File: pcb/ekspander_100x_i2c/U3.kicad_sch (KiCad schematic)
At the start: 21 parts, among them J10 DG127A-5.08-06P-14-00AH, J11 DG127A-5.08-06P-14-00AH, J8 DG127A-5.08-06P-14-00AH, J9 DG127A-5.08-06P-14-00AH, U19 LTV-847, U20 LTV-847, U21 ITS716G, U22 ITS716G, U23 ITS716G, U24 ITS716G, U25 LTV-847, U3 MCP23017_SP, U4 MCP23017_SP

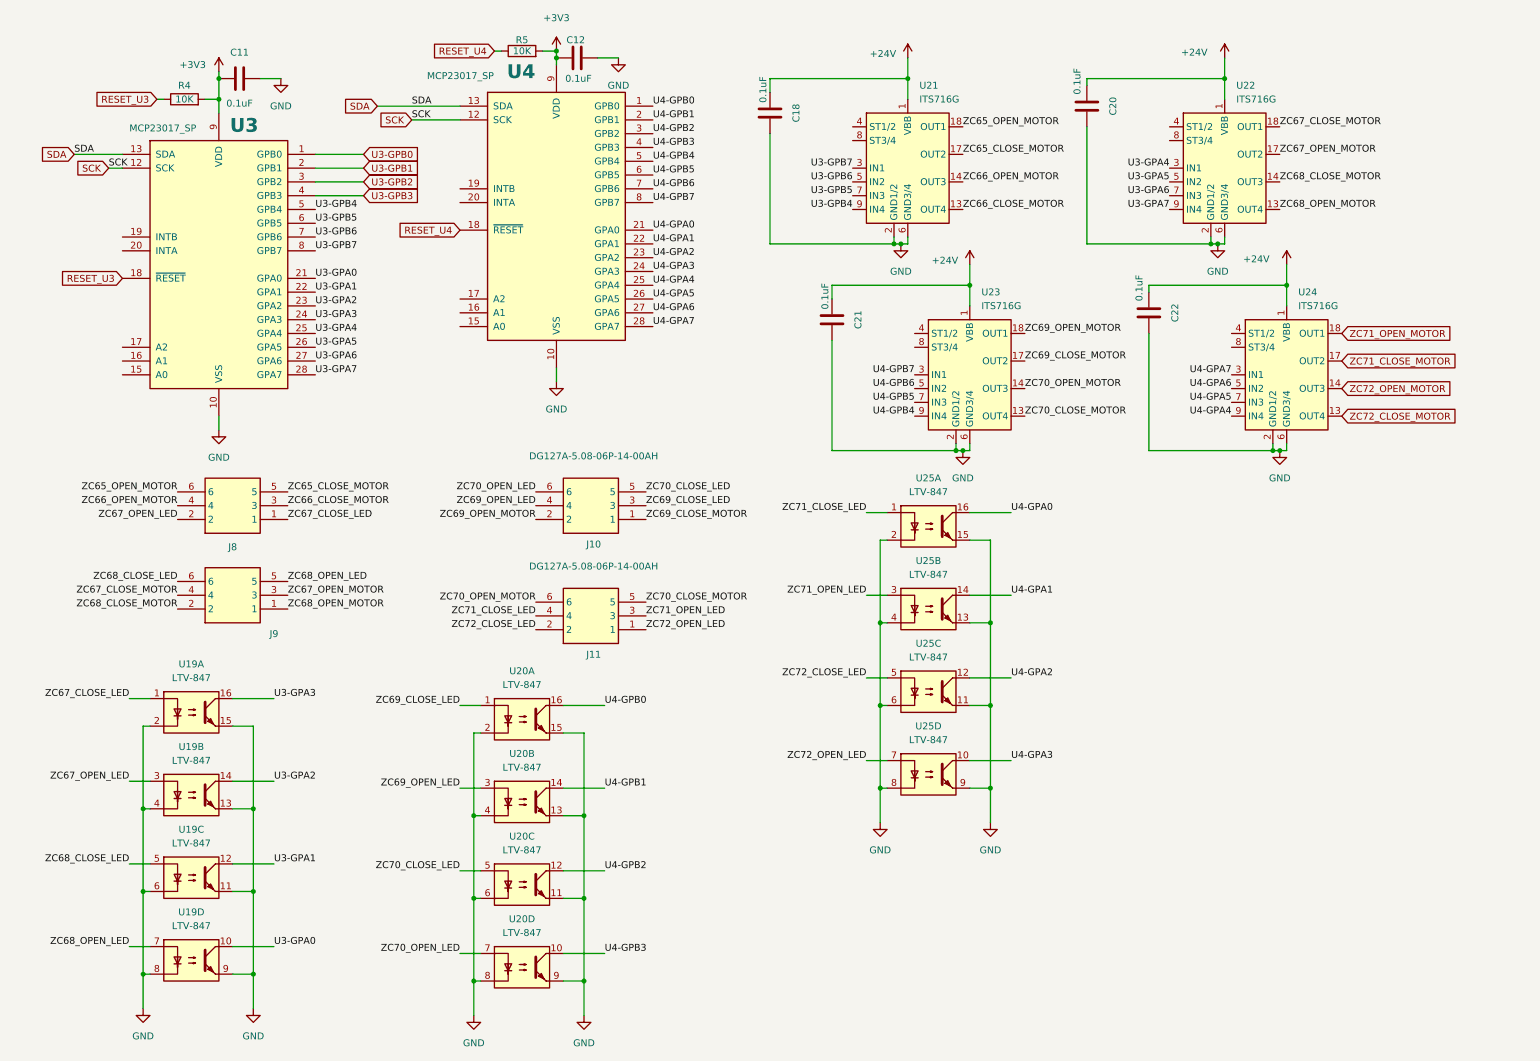
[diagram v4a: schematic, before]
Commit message: Ekspander 100x - finish J
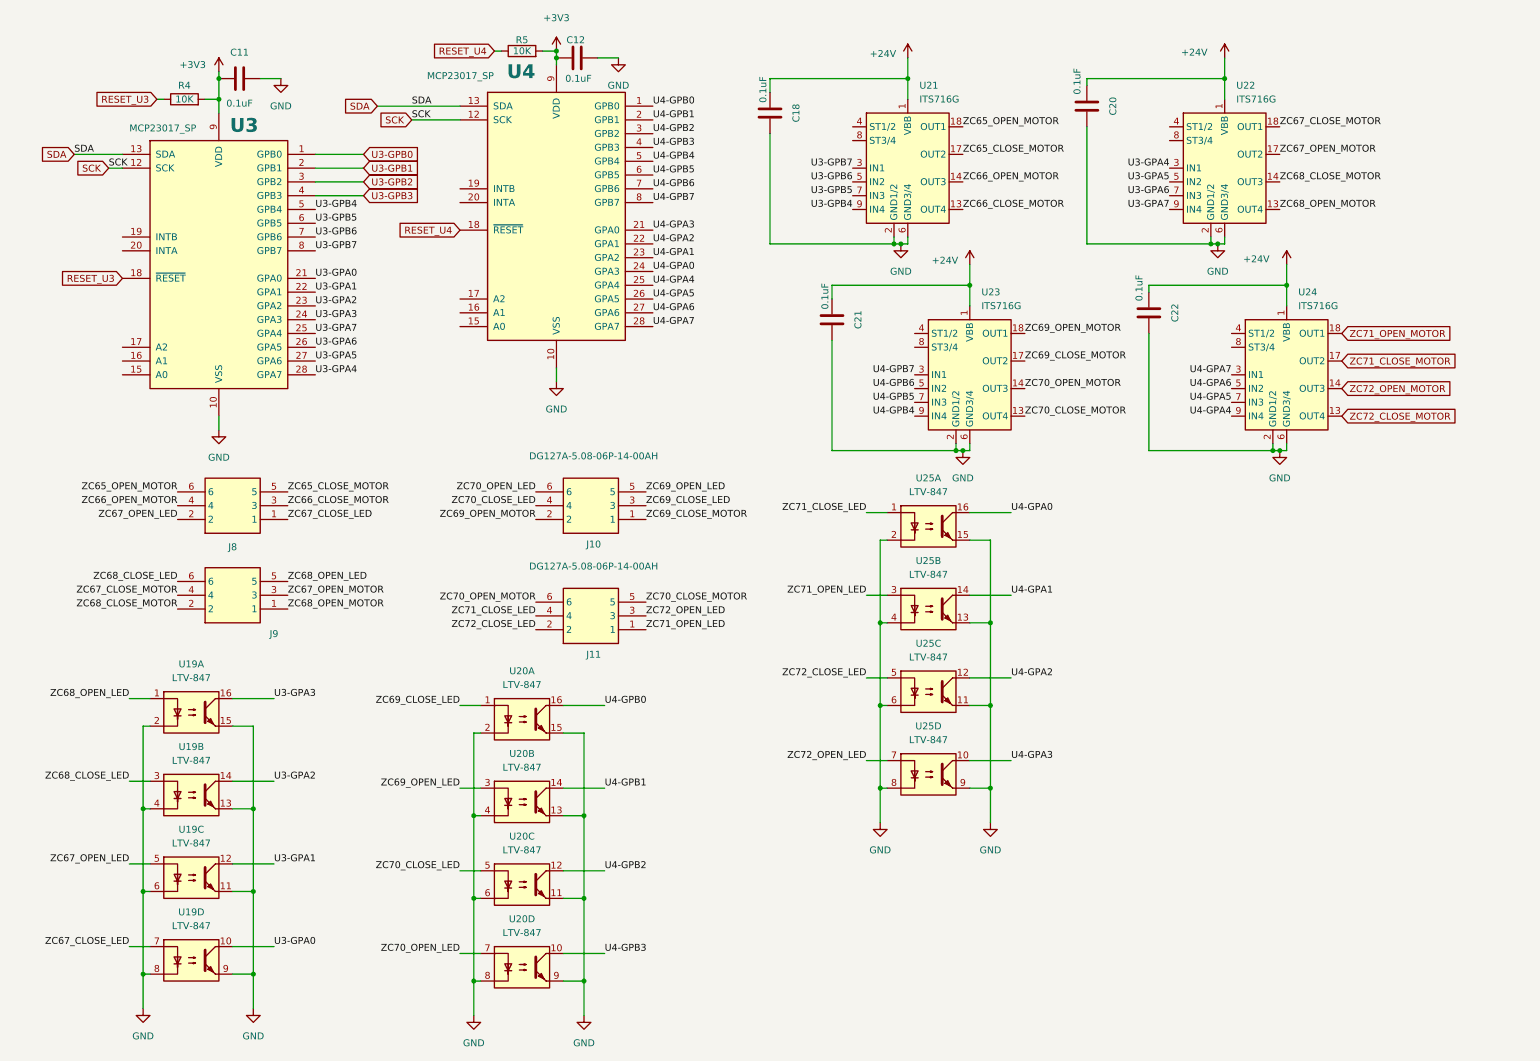
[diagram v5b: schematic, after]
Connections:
- net U3-GPA4: now also U3.28 (GPA7); no longer U3.25 (GPA4)
- net U3-GPA5: now also U3.27 (GPA6); no longer U3.26 (GPA5)
- net U3-GPA6: now also U3.26 (GPA5); no longer U3.27 (GPA6)
- net U3-GPA7: now also U3.25 (GPA4); no longer U3.28 (GPA7)
- net U4-GPA0: now also U4.24 (GPA3); no longer U4.21 (GPA0)
- net U4-GPA1: now also U4.23 (GPA2); no longer U4.22 (GPA1)
- net U4-GPA2: now also U4.22 (GPA1); no longer U4.23 (GPA2)
- net U4-GPA3: now also U4.21 (GPA0); no longer U4.24 (GPA3)
- net ZC67_CLOSE_LED: now also U19.7; no longer U19.1
- net ZC67_OPEN_LED: now also U19.5; no longer U19.3
- net ZC68_CLOSE_LED: now also U19.3; no longer U19.5
- net ZC68_OPEN_LED: now also U19.1; no longer U19.7
- net ZC69_OPEN_LED: now also J10.5; no longer J10.4
- net ZC70_CLOSE_LED: now also J10.4; no longer J10.5
- net ZC71_OPEN_LED: now also J11.1; no longer J11.3
- net ZC72_OPEN_LED: now also J11.3; no longer J11.1
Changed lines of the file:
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@@
 	)
 	(label "ZC70_CLOSE_LED"
-		(at 124.46 96.52 0)
-		(effects
-			(font
-				(size 1.27 1.27)
-			)
-			(justify left bottom)
+		(at 104.14 99.06 180)
+		(effects
+			(font
+				(size 1.27 1.27)
+			)
+			(justify right bottom)
 		)
 	)
@@
 	)
 	(label "U4-GPA0"
-		(at 125.73 48.26 0)
-		(effects
-			(font
-				(size 1.27 1.27)
-			)
-			(justify left bottom)
-		)
-		(property "Netclass" "GPIO"
-			(at 135.89 48.26 0)
+		(at 125.73 55.88 0)
+		(effects
+			(font
+				(size 1.27 1.27)
+			)
+			(justify left bottom)
+		)
+		(property "Netclass" "GPIO"
+			(at 135.89 55.88 0)
 			(effects
 				(font
@@
 	)
 	(label "ZC67_OPEN_LED"
-		(at 29.21 149.86 180)
+		(at 29.21 165.1 180)
 		(effects
 			(font
@@
 	)
 	(label "ZC72_OPEN_LED"
-		(at 124.46 121.92 0)
+		(at 124.46 119.38 0)
 		(effects
 			(font
@@
 	)
 	(label "U3-GPA5"
-		(at 63.5 69.85 0)
-		(effects
-			(font
-				(size 1.27 1.27)
-			)
-			(justify left bottom)
-		)
-		(property "Netclass" "GPIO"
-			(at 73.406 69.85 0)
+		(at 63.5 72.39 0)
+		(effects
+			(font
+				(size 1.27 1.27)
+			)
+			(justify left bottom)
+		)
+		(property "Netclass" "GPIO"
+			(at 73.406 72.39 0)
 			(effects
 				(font
@@
 	)
 	(label "U3-GPA7"
-		(at 63.5 74.93 0)
-		(effects
-			(font
-				(size 1.27 1.27)
-			)
-			(justify left bottom)
-		)
-		(property "Netclass" "GPIO"
-			(at 73.406 74.93 0)
+		(at 63.5 67.31 0)
+		(effects
+			(font
+				(size 1.27 1.27)
+			)
+			(justify left bottom)
+		)
+		(property "Netclass" "GPIO"
+			(at 73.406 67.31 0)
 			(effects
 				(font
@@
 	)
 	(label "U4-GPA2"
-		(at 125.73 53.34 0)
-		(effects
-			(font
-				(size 1.27 1.27)
-			)
-			(justify left bottom)
-		)
-		(property "Netclass" "GPIO"
-			(at 135.636 53.34 0)
+		(at 125.73 50.8 0)
+		(effects
+			(font
+				(size 1.27 1.27)
+			)
+			(justify left bottom)
+		)
+		(property "Netclass" "GPIO"
+			(at 135.636 50.8 0)
 			(effects
 				(font
@@
 	)
 	(label "ZC68_CLOSE_LED"
-		(at 29.21 165.1 180)
+		(at 29.21 149.86 180)
 		(effects
 			(font
@@
 	)
 	(label "ZC68_OPEN_LED"
-		(at 29.21 180.34 180)
+		(at 29.21 134.62 180)
 		(effects
 			(font
@@
 	)
 	(label "U3-GPA4"
-		(at 63.5 67.31 0)
-		(effects
-			(font
-				(size 1.27 1.27)
-			)
-			(justify left bottom)
-		)
-		(property "Netclass" "GPIO"
-			(at 73.406 67.31 0)
+		(at 63.5 74.93 0)
+		(effects
+			(font
+				(size 1.27 1.27)
+			)
+			(justify left bottom)
+		)
+		(property "Netclass" "GPIO"
+			(at 73.406 74.93 0)
 			(effects
 				(font
@@
 	)
 	(label "U3-GPA6"
-		(at 63.5 72.39 0)
-		(effects
-			(font
-				(size 1.27 1.27)
-			)
-			(justify left bottom)
-		)
-		(property "Netclass" "GPIO"
-			(at 73.406 72.39 0)
+		(at 63.5 69.85 0)
+		(effects
+			(font
+				(size 1.27 1.27)
+			)
+			(justify left bottom)
+		)
+		(property "Netclass" "GPIO"
+			(at 73.406 69.85 0)
 			(effects
 				(font
@@
 	)
 	(label "ZC67_CLOSE_LED"
-		(at 29.21 134.62 180)
+		(at 29.21 180.34 180)
 		(effects
 			(font
@@
 	)
 	(label "U4-GPA3"
-		(at 125.73 55.88 0)
-		(effects
-			(font
-				(size 1.27 1.27)
-			)
-			(justify left bottom)
-		)
-		(property "Netclass" "GPIO"
-			(at 135.636 55.88 0)
+		(at 125.73 48.26 0)
+		(effects
+			(font
+				(size 1.27 1.27)
+			)
+			(justify left bottom)
+		)
+		(property "Netclass" "GPIO"
+			(at 135.636 48.26 0)
 			(effects
 				(font
@@
 	)
 	(label "ZC71_OPEN_LED"
-		(at 124.46 119.38 0)
+		(at 124.46 121.92 0)
 		(effects
 			(font
@@
 	)
 	(label "U4-GPA1"
-		(at 125.73 50.8 0)
-		(effects
-			(font
-				(size 1.27 1.27)
-			)
-			(justify left bottom)
-		)
-		(property "Netclass" "GPIO"
-			(at 135.89 50.8 0)
+		(at 125.73 53.34 0)
+		(effects
+			(font
+				(size 1.27 1.27)
+			)
+			(justify left bottom)
+		)
+		(property "Netclass" "GPIO"
+			(at 135.89 53.34 0)
 			(effects
 				(font
@@
 	)
 	(label "ZC69_OPEN_LED"
-		(at 104.14 99.06 180)
-		(effects
-			(font
-				(size 1.27 1.27)
-			)
-			(justify right bottom)
-		)
-	)
+		(at 124.46 96.52 0)
+		(effects
+			(font
+				(size 1.27 1.27)
+			)
+			(justify left bottom)
+		)
+	)

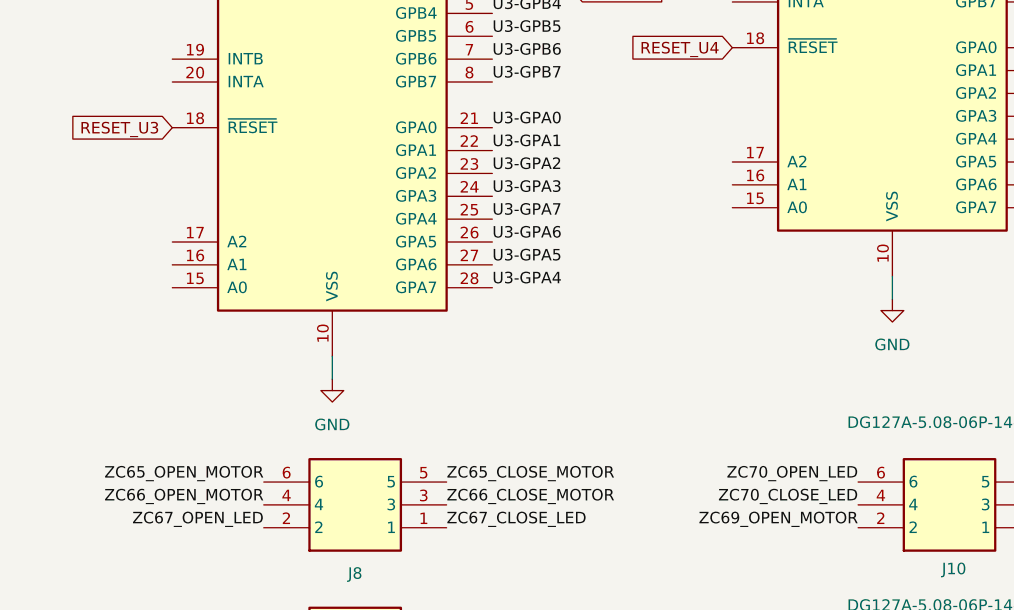
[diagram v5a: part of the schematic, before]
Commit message: Ekspander 100x - adresacja I2C - MCP23017
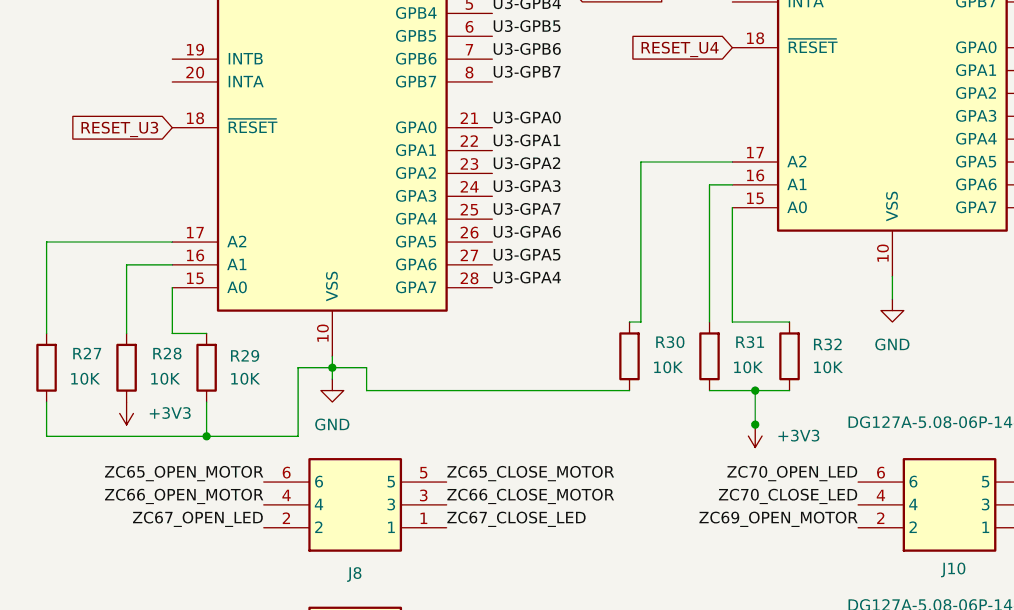
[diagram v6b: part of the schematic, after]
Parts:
- added R27, R28, R29, R30, R31, R32: 10K, PCM_Resistor_SMD_AKL:R_0805_2012Metric_Pad1.20x1.40mm_HandSolder, symbol Device:R
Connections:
- net +3V3: now also R28.1, R31.1, R32.1
- net GND: now also R27.1, R29.1, R30.1
- net at U3.15 (A0): now also R29.2
- net at U3.16 (A1): now also R28.2
- net at U3.17 (A2): now also R27.2
- net at U4.15 (A0): now also R32.2
- net at U4.16 (A1): now also R31.2
- net at U4.17 (A2): now also R30.2

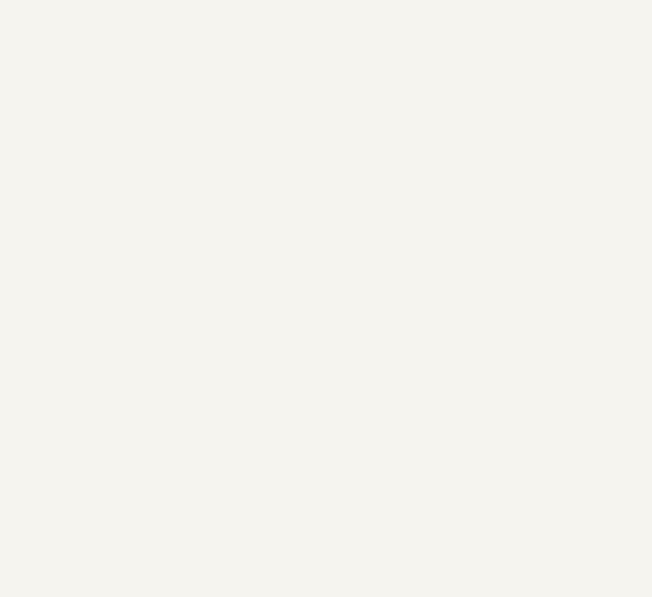
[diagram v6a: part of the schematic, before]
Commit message: Ekspander 100x - mounting holes - rerouting
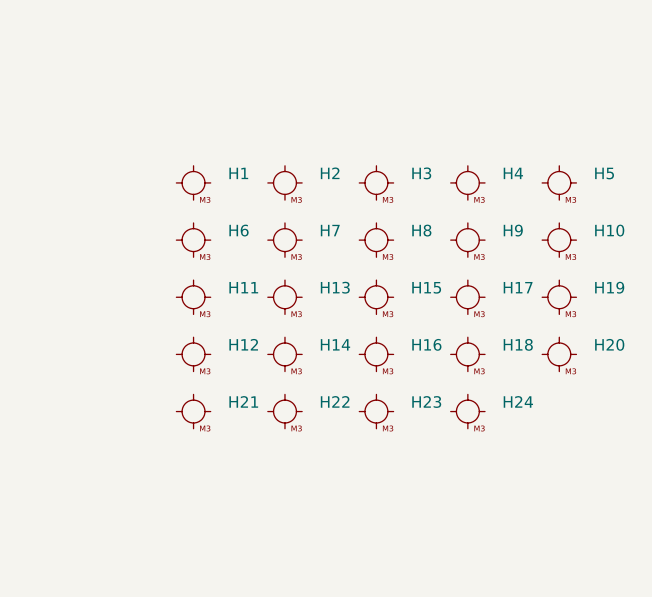
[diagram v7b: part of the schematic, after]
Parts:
- added H1, H10, H11, H12, H13, H14, H15, H16, H17, H18, H19, H2, H20, H21, H22, H23, H24, H3, H4, H5, H6, H7, H8, H9: ~, PCM_fab:MountingHole_M3, symbol PCM_fab:MountingHole_M3
